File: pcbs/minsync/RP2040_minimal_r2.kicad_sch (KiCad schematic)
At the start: 39 parts, among them J1 Comm, J2 Comm, J3 Comm, J4 Comm, J5 SWD_CONN, J6 Conn_01x01_Pin, J7 SSD1306, SW1 SW_Push, U1 NCP1117-3.3_SOT223, U2 W25Q128JVS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

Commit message: Get minsync PCB ready for order
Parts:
- added C2: 100n, Capacitor_SMD:C_0402_1005Metric, symbol Device:C
- added TP2: TestPoint, Connector_PinHeader_2.54mm:PinHeader_1x01_P2.54mm_Vertical, symbol Connector:TestPoint
- renumbered J1 to PTP1, J2 to PTP2, J3 to PTP3, J4 to PTP4
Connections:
- net +3V3: now also C2.1; no longer U4.1 (VDD)
- net SI_CLK2: now also TP2.1
- new net: C2.2, U4.1 (VDD)
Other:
- note added: "TODO: x check BOOTSEL button: compare to RPi Pico x check if screen would actually fit x check RUN pin with rp minimal change LED in BOM to a better color (C2290?) x fix tiny trace error to the right of rp2040 check the exact components for the whole BOM"
- note removed: "TODO: x check BOOTSEL button: compare to RPi Pico x check if screen would actually fit x check RUN pin with rp minimal change LED in BOM to a better color (C2290?) fix tiny trace error to the right of rp2040"
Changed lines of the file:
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@@
 		)
 	)
-	(text "TODO:\nx check BOOTSEL button: compare to RPi Pico\nx check if screen would actually fit\nx check RUN pin with rp minimal\nchange LED in BOM to a better color (C2290?)\nfix tiny trace error to the right of rp2040"
+	(text "TODO:\nx check BOOTSEL button: compare to RPi Pico\nx check if screen would actually fit\nx check RUN pin with rp minimal\nchange LED in BOM to a better color (C2290?)\nx fix tiny trace error to the right of rp2040\ncheck the exact components for the whole BOM"
 		(exclude_from_sim no)
 		(at 146.558 24.13 0)
@@
 		)
 	)
+	(label "SI_CLK2"
+		(at 88.9 275.59 0)
+		(fields_autoplaced yes)
+		(effects
+			(font
+				(size 1.27 1.27)
+			)
+			(justify left bottom)
+		)
+	)
 	(label "GPIO24"
 		(at 386.08 86.36 0)
@@
 		(dnp no)
 		(fields_autoplaced yes)
-		(property "Reference" "J4"
+		(property "Reference" "PTP4"
 			(at 379.73 80.01 0)
 			(effects
@@
 			(project "RP2040_minimal_r2"
 				(path "/8c0b3d8b-46d3-4173-ab1e-a61765f77d61"
-					(reference "J4")
+					(reference "PTP4")
 					(unit 1)
 				)
@@
 	)
 	(symbol
+		(lib_id "Device:C")
+		(at 85.09 218.44 0)
+		(unit 1)
+		(exclude_from_sim no)
+		(in_bom yes)
+		(on_board yes)
+		(dnp no)
+		(property "Reference" "C2"
+			(at 88.011 217.2716 0)
+			(effects
+				(font
+					(size 1.27 1.27)
+				)
+				(justify left)
+			)
+		)
+		(property "Value" "100n"
+			(at 88.011 219.583 0)
+			(effects
+				(font
+					(size 1.27 1.27)
+				)
+				(justify left)
+			)
+		)
+		(property "Footprint" "Capacitor_SMD:C_0402_1005Metric"
+			(at 86.0552 222.25 0)
+			(effects
+				(font
+					(size 1.27 1.27)
+				)
+				(hide yes)
+			)
+		)
+		(property "Datasheet" "~"
+			(at 85.09 218.44 0)
+			(effects
+				(font
+					(size 1.27 1.27)
+				)
+				(hide yes)
+			)
+		)
+		(property "Description" ""
+			(at 85.09 218.44 0)
+			(effects
+				(font
+					(size 1.27 1.27)
+				)
+				(hide yes)
+			)
+		)
+		(pin "1"
+		)
+		(pin "2"
+		)
+		(instances
+			(project "RP2040_minimal_r2"
+				(path "/8c0b3d8b-46d3-4173-ab1e-a61765f77d61"
+					(reference "C2")
+					(unit 1)
+				)
+			)
+		)
+	)
+	(symbol
 		(lib_id "Connector_Generic:Conn_01x03")
 		(at 308.61 36.83 180)
@@
 		(dnp no)
 		(fields_autoplaced yes)
-		(property "Reference" "J3"
+		(property "Reference" "PTP3"
 			(at 379.73 60.96 0)
 			(effects
@@
 			(project "RP2040_minimal_r2"
 				(path "/8c0b3d8b-46d3-4173-ab1e-a61765f77d61"
-					(reference "J3")
+					(reference "PTP3")
 					(unit 1)
 				)
@@
 		(dnp no)
 		(fields_autoplaced yes)
-		(property "Reference" "J1"
+		(property "Reference" "PTP1"
 			(at 379.73 20.32 0)
 			(effects
@@
 			(project ""
 				(path "/8c0b3d8b-46d3-4173-ab1e-a61765f77d61"
-					(reference "J1")
+					(reference "PTP1")
 					(unit 1)
 				)
@@
 		(dnp no)
 		(fields_autoplaced yes)
-		(property "Reference" "J2"
+		(property "Reference" "PTP2"
 			(at 379.73 41.91 0)
 			(effects
@@
 			(project "RP2040_minimal_r2"
 				(path "/8c0b3d8b-46d3-4173-ab1e-a61765f77d61"
-					(reference "J2")
+					(reference "PTP2")
+					(unit 1)
+				)
+			)
+		)
+	)
+	(symbol
+		(lib_id "Connector:TestPoint")
+		(at 88.9 275.59 90)
+		(unit 1)
+		(exclude_from_sim no)
+		(in_bom yes)
+		(on_board yes)
+		(dnp no)
+		(fields_autoplaced yes)
+		(property "Reference" "TP2"
+			(at 85.598 270.51 90)
+			(effects
+				(font
+					(size 1.27 1.27)
+				)
+			)
+		)
+		(property "Value" "TestPoint"
+			(at 85.598 273.05 90)
+			(effects
+				(font
+					(size 1.27 1.27)
+				)
+			)
+		)
+		(property "Footprint" "Connector_PinHeader_2.54mm:PinHeader_1x01_P2.54mm_Vertical"
+			(at 88.9 270.51 0)
+			(effects
+				(font
+					(size 1.27 1.27)
+				)
+				(hide yes)
+			)
+		)
+		(property "Datasheet" "~"
+			(at 88.9 270.51 0)
+			(effects
+				(font
+					(size 1.27 1.27)
+				)
+				(hide yes)
+			)
+		)
+		(property "Description" "test point"
+			(at 88.9 275.59 0)
+			(effects
+				(font
+					(size 1.27 1.27)
+				)
+				(hide yes)
+			)
+		)
+		(pin "1"
+		)
+		(instances
+			(project "RP2040_minimal_r2"
+				(path "/8c0b3d8b-46d3-4173-ab1e-a61765f77d61"
+					(reference "TP2")
 					(unit 1)
 				)
@@
 	(symbol
 		(lib_id "power:+3V3")
-		(at 85.09 222.25 0)
+		(at 85.09 214.63 0)
 		(unit 1)
 		(exclude_from_sim no)
@@
 		(dnp no)
 		(property "Reference" "#PWR045"
-			(at 85.09 226.06 0)
+			(at 85.09 218.44 0)
 			(effects
 				(font
@@
 		)
 		(property "Value" "+3V3"
-			(at 85.471 217.8558 0)
+			(at 85.471 210.2358 0)
 			(effects
 				(font
@@
 		)
 		(property "Footprint" ""
-			(at 85.09 222.25 0)
+			(at 85.09 214.63 0)
 			(effects
 				(font
@@
 		)
 		(property "Datasheet" ""
-			(at 85.09 222.25 0)
+			(at 85.09 214.63 0)
 			(effects
 				(font
@@
 		)
 		(property "Description" ""
-			(at 85.09 222.25 0)
+			(at 85.09 214.63 0)
 			(effects
 				(font

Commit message: Pos changes
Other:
- note added: "TODO: x check BOOTSEL button: compare to RPi Pico x check if screen would actually fit x check RUN pin with rp minimal x change LED in BOM to a better color (C2290?) x fix tiny trace error to the right of rp2040 x check the exact components for the whole BOM"
- note removed: "TODO: x check BOOTSEL button: compare to RPi Pico x check if screen would actually fit x check RUN pin with rp minimal change LED in BOM to a better color (C2290?) x fix tiny trace error to the right of rp2040 check the exact components for the whole BOM"
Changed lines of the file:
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@@
 		)
 	)
-	(text "TODO:\nx check BOOTSEL button: compare to RPi Pico\nx check if screen would actually fit\nx check RUN pin with rp minimal\nchange LED in BOM to a better color (C2290?)\nx fix tiny trace error to the right of rp2040\ncheck the exact components for the whole BOM"
+	(text "TODO:\nx check BOOTSEL button: compare to RPi Pico\nx check if screen would actually fit\nx check RUN pin with rp minimal\nx change LED in BOM to a better color (C2290?)\nx fix tiny trace error to the right of rp2040\nx check the exact components for the whole BOM"
 		(exclude_from_sim no)
 		(at 146.558 24.13 0)

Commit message: Debug minsync PCB
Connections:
- net at C2.2, U4.1 (VDD): now also U4.7 (VDDO)
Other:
- note added: "TODO: Si5351: "Unused VDDO pins should be tied to VDD" board-to-board connector for SWD can exist together with headers Does the screen work? Can the board run programs for a long time?"
- note removed: "TODO: x check BOOTSEL button: compare to RPi Pico x check if screen would actually fit x check RUN pin with rp minimal x change LED in BOM to a better color (C2290?) x fix tiny trace error to the right of rp2040 x check the exact components for the whole BOM"
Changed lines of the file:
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@@
 	)
 	(junction
+		(at 85.09 222.25)
+		(diameter 0)
+		(color 0 0 0 0)
+	)
+	(junction
 		(at 223.52 60.96)
 		(diameter 0)
@@
 	(wire
 		(pts
+			(xy 85.09 222.25) (xy 90.17 222.25)
+		)
+		(stroke
+			(width 0)
+			(type default)
+		)
+	)
+	(wire
+		(pts
 			(xy 204.47 93.98) (xy 204.47 81.28)
 		)
@@
 		)
 	)
-	(text "TODO:\nx check BOOTSEL button: compare to RPi Pico\nx check if screen would actually fit\nx check RUN pin with rp minimal\nx change LED in BOM to a better color (C2290?)\nx fix tiny trace error to the right of rp2040\nx check the exact components for the whole BOM"
+	(text "TODO:\nSi5351: \"Unused VDDO pins should be tied to VDD\"\nboard-to-board connector for SWD can exist together with headers\nDoes the screen work?\nCan the board run programs for a long time?"
 		(exclude_from_sim no)
 		(at 146.558 24.13 0)
@@
 		(dnp no)
 		(property "Reference" "C2"
-			(at 88.011 217.2716 0)
+			(at 76.962 217.3986 0)
 			(effects
 				(font
@@
 		)
 		(property "Value" "100n"
-			(at 88.011 219.583 0)
+			(at 76.962 219.71 0)
 			(effects
 				(font

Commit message: Add todo's
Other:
- note added: "TODO: Si5351: "Unused VDDO pins should be tied to VDD" board-to-board connector for SWD can exist together with headers Does the screen work? Can the board run programs for a long time? Reverse engineer Si5351 dev board and compare Re-order vias for north connector Less bright LED?"
- note removed: "TODO: Si5351: "Unused VDDO pins should be tied to VDD" board-to-board connector for SWD can exist together with headers Does the screen work? Can the board run programs for a long time?"
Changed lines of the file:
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@@
 		)
 	)
-	(text "TODO:\nSi5351: \"Unused VDDO pins should be tied to VDD\"\nboard-to-board connector for SWD can exist together with headers\nDoes the screen work?\nCan the board run programs for a long time?"
+	(text "TODO:\nSi5351: \"Unused VDDO pins should be tied to VDD\"\nboard-to-board connector for SWD can exist together with headers\nDoes the screen work?\nCan the board run programs for a long time?\nReverse engineer Si5351 dev board and compare\nRe-order vias for north connector\nLess bright LED?"
 		(exclude_from_sim no)
-		(at 146.558 24.13 0)
+		(at 147.574 28.194 0)
 		(effects
 			(font
 				(size 1.27 1.27)
 			)
-			(justify left)
+			(justify left top)
 		)
 	)

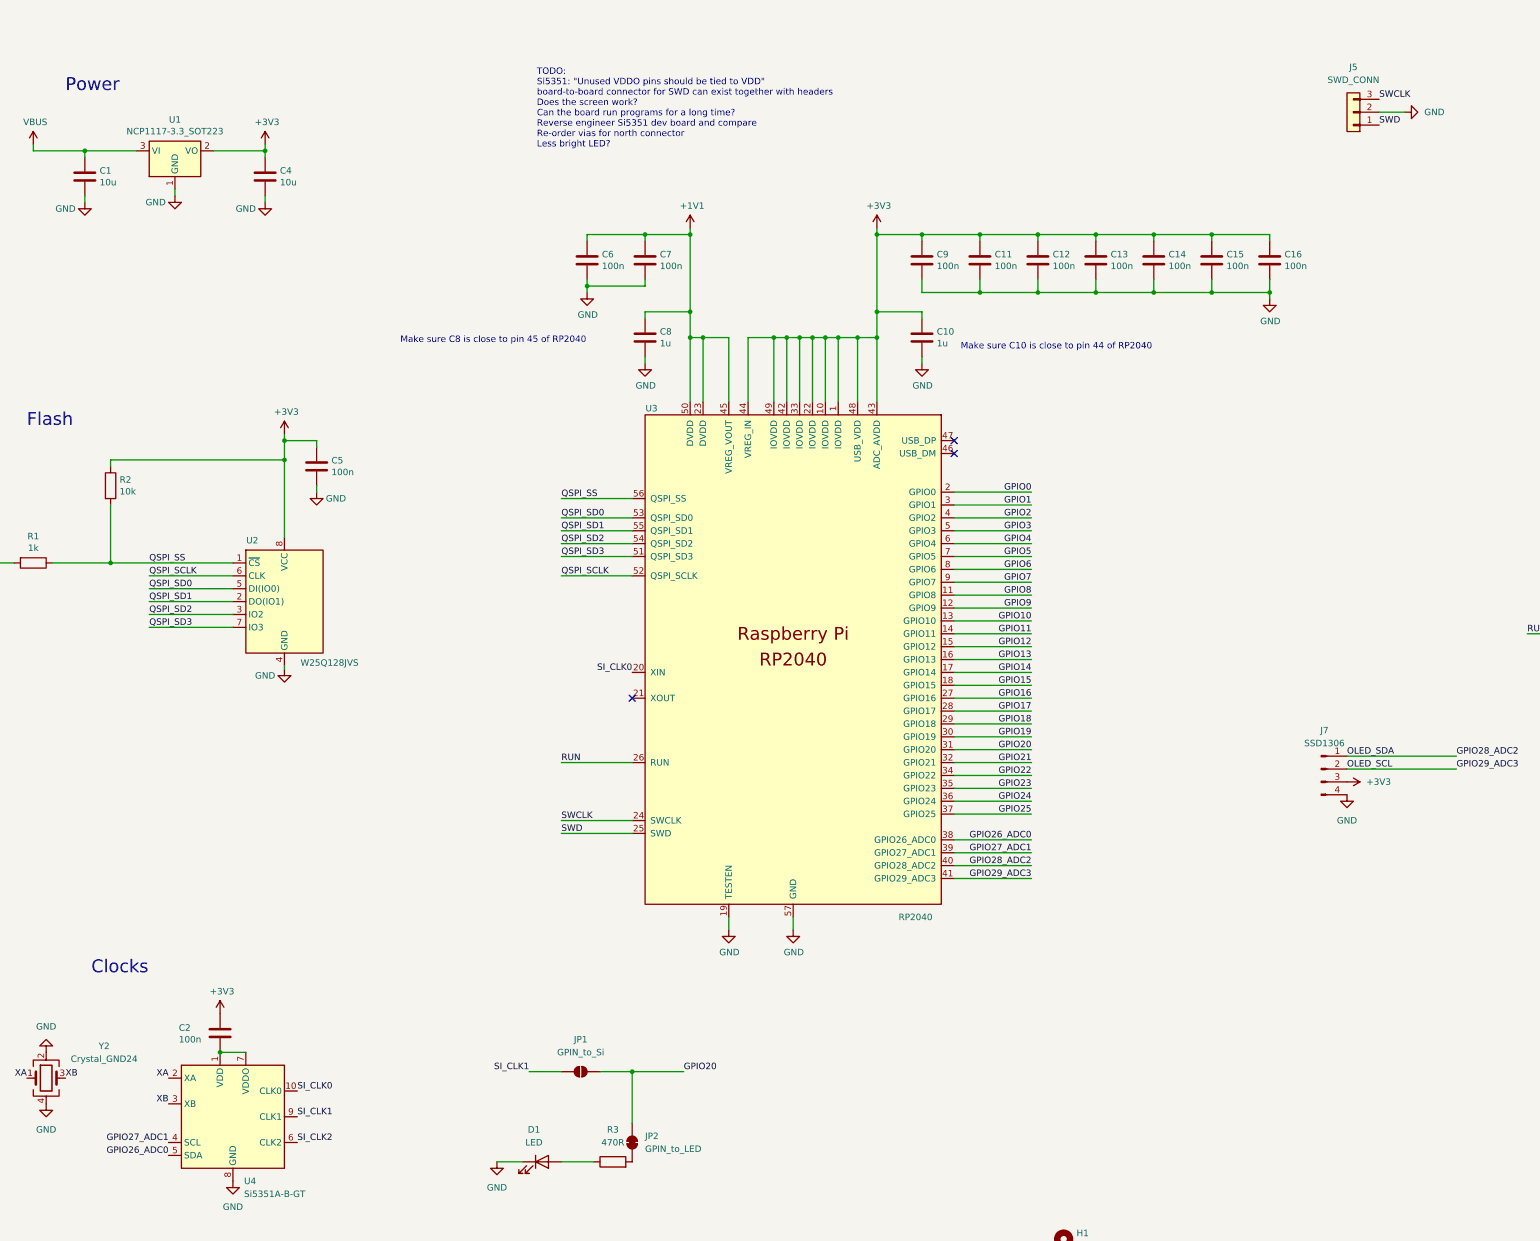
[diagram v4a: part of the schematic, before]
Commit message: Test more of the hardware / make PCB modifications for v0.2
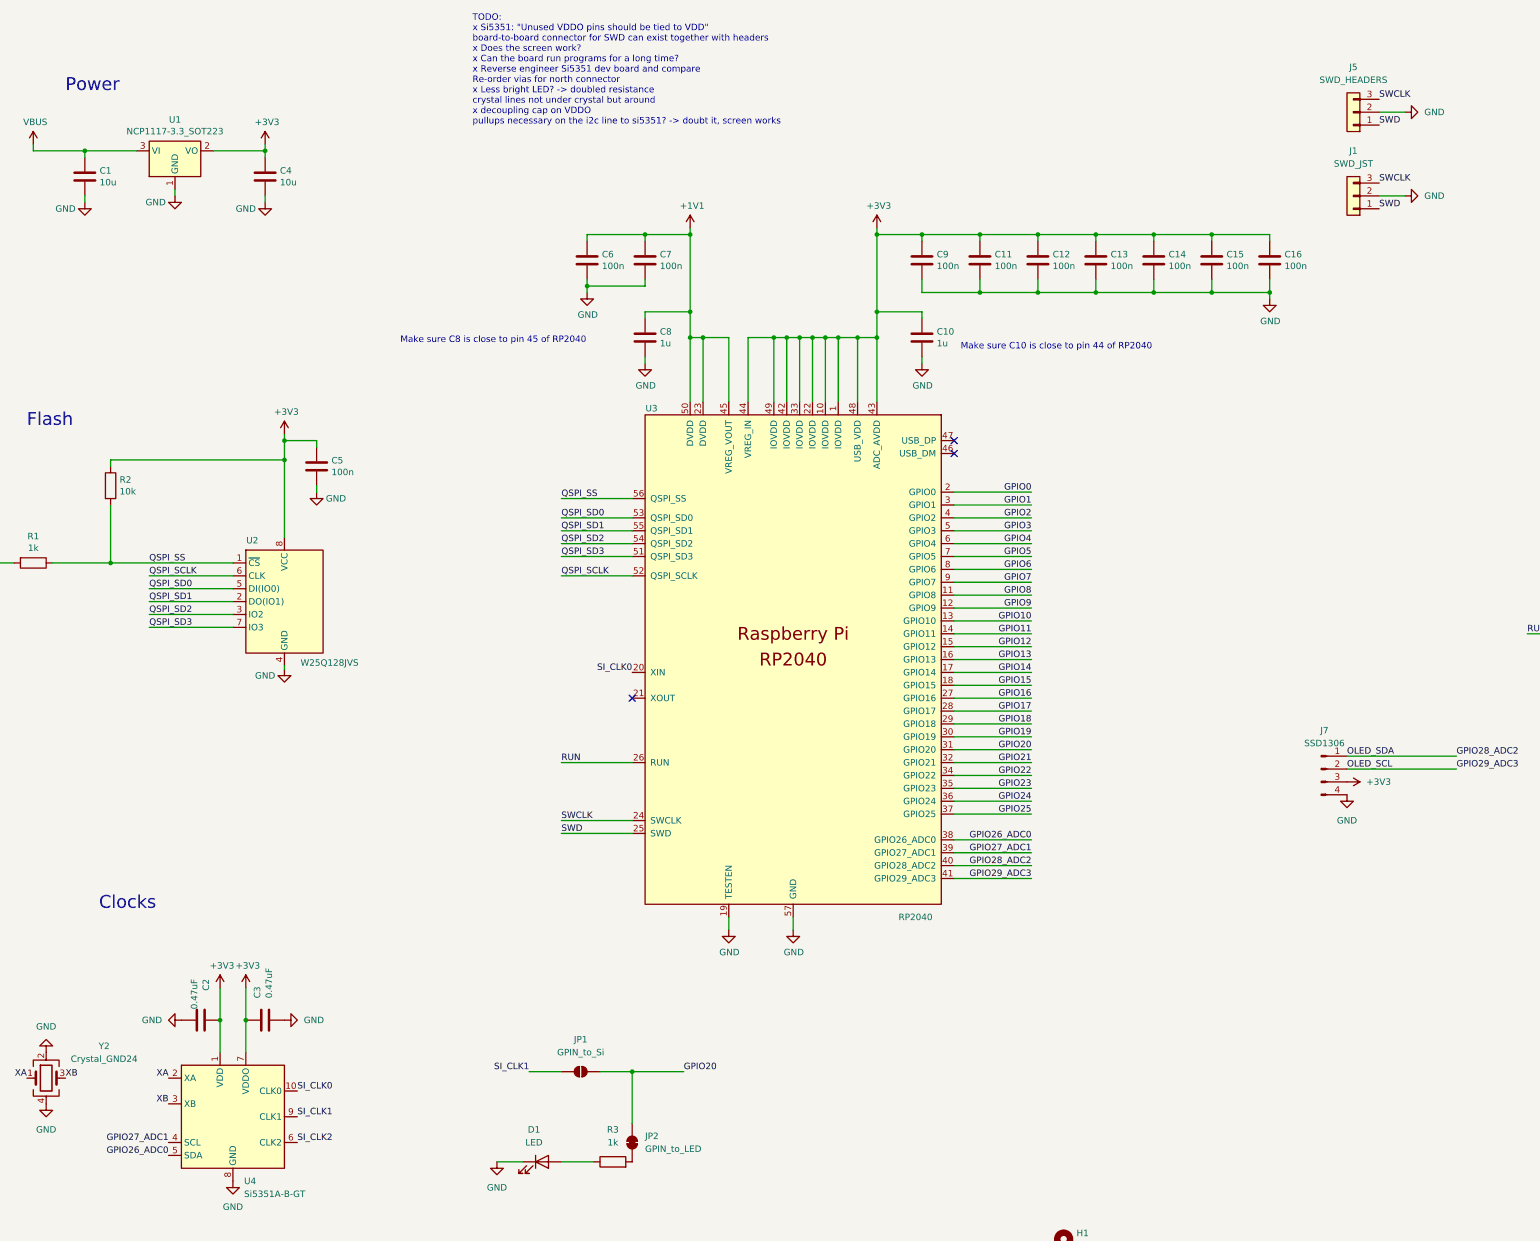
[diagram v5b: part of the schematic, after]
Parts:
- added C3: 0.47uF, Capacitor_SMD:C_0402_1005Metric, symbol Device:C
- added J1: SWD_JST, symbol Connector_Generic:Conn_01x03
- C2: value 100n -> 0.47uF
- J5: value SWD_CONN -> SWD_HEADERS
- R3: value 470R -> 1k
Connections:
- net +3V3: now also U4.1 (VDD), U4.7 (VDDO), C3.1
- net GND: now also C2.2, C3.2, J1.2 (Pin_2)
- net SWCLK: now also J1.3 (Pin_3)
- net SWD: now also J1.1 (Pin_1)
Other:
- note added: "TODO: x Si5351: "Unused VDDO pins should be tied to VDD" board-to-board connector for SWD can exist together with headers x Does the screen work? x Can the board run programs for a long time? x Reverse engineer Si5351 dev board and compare Re-order vias for north connector x Less bright LED? -> doubled resistance crystal lines not under crystal but around x decoupling cap on VDDO pullups necessar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"
- note removed: "TODO: Si5351: "Unused VDDO pins should be tied to VDD" board-to-board connector for SWD can exist together with headers Does the screen work? Can the board run programs for a long time? Reverse engineer Si5351 dev board and compare Re-order vias for north connector Less bright LED?"
- moved on the sheet: C2
